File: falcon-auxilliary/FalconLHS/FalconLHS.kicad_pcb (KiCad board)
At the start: 2 copper layers, 85.7 x 57.5 mm, 18 parts, among them J1 100mil, U1 AL8843QSP-13, U2 AL8843QSP-13

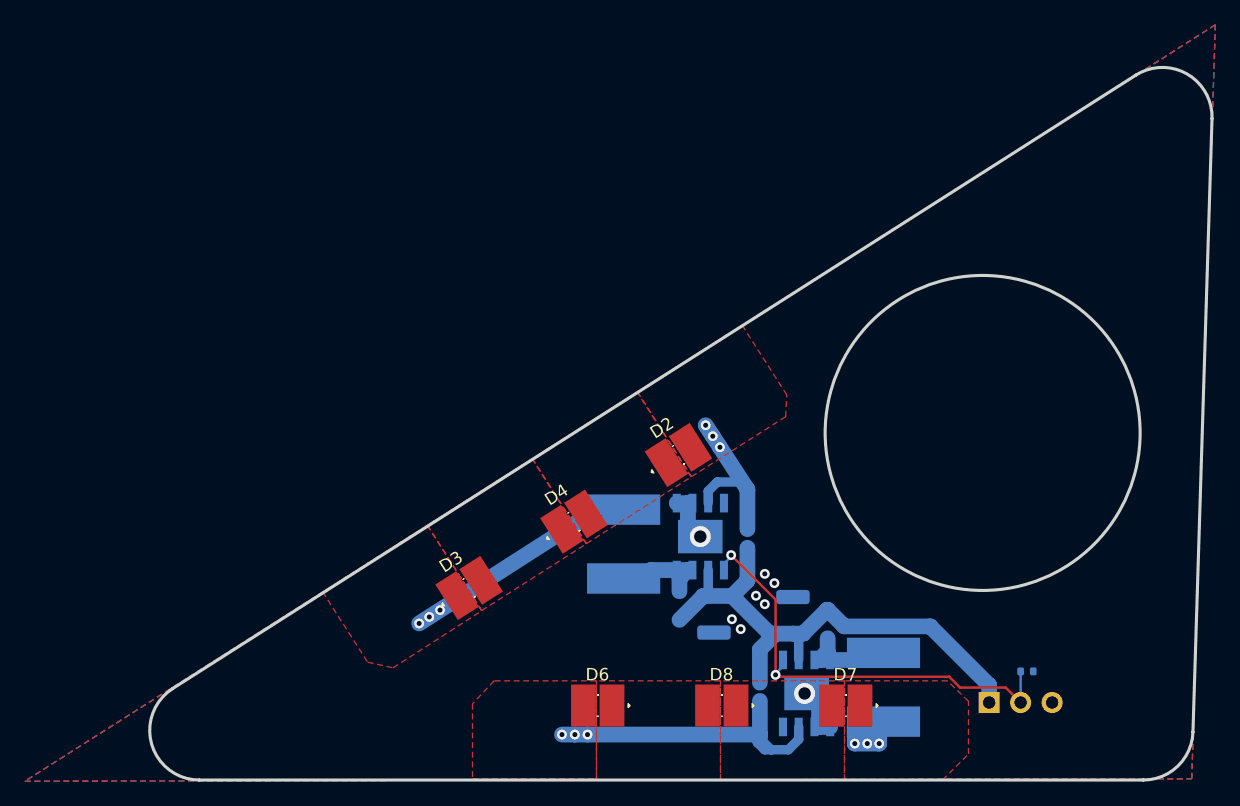
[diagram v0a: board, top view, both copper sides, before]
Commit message: Fix missing mounting holes
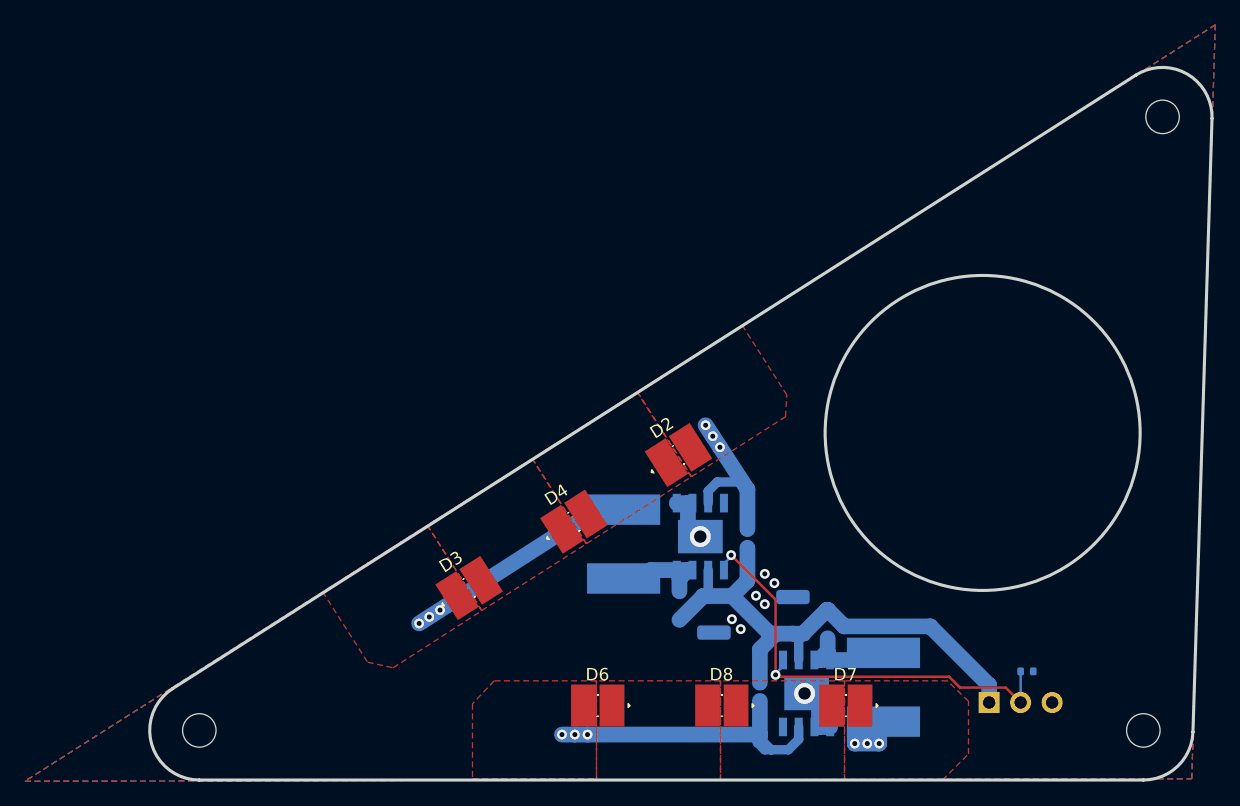
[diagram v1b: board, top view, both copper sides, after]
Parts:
- added H1: MountingHole, JetkovKiCADLib:MountingHole_2.7mm_M2.5_Clearanced, F.Cu at (109.0, 124.0)
- added H2: MountingHole, JetkovKiCADLib:MountingHole_2.7mm_M2.5_Clearanced, F.Cu at (186.7, 74.5)
- added H3: MountingHole, JetkovKiCADLib:MountingHole_2.7mm_M2.5_Clearanced, F.Cu at (185.1, 124.0)
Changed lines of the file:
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@@
     )
+  )
+  (footprint "JetkovKiCADLib:MountingHole_2.7mm_M2.5_Clearanced" locked (layer "F.Cu")
+    (at 185.125 124)
+    (descr "Mounting Hole 2.7mm, no annular, M2.5")
+    (tags "mounting hole 2.7mm no annular m2.5")
+    (property "Sheetfile" "FalconLHS.kicad_sch")
+    (property "Sheetname" "")
+    (clearance 1.5)
+    (attr exclude_from_pos_files)
+    (fp_text reference "H3" (at 0 -3.7) (layer "F.SilkS") hide
+      (effects (font (size 1 1) (thickness 0.15)))
+    )
+    (fp_text value "MountingHole" (at 0 3.7) (layer "F.Fab")
+      (effects (font (size 1 1) (thickness 0.15)))
+    )
+    (fp_text user "${REFERENCE}" (at 0.3 0) (layer "F.Fab")
+      (effects (font (size 1 1) (thickness 0.15)))
+    )
+    (fp_circle (center 0 0) (end 2.7 0) (layer "Cmts.User") (width 0.15) (fill none))
+    (fp_circle (center 0 0) (end 2.95 0) (layer "F.CrtYd") (width 0.05) (fill none))
+    (pad "" np_thru_hole circle locked (at 0 0) (size 2.7 2.7) (drill 2.7) (layers F&B.Cu *.Mask)
+      (clearance 1.5))
+  )
+  (footprint "JetkovKiCADLib:MountingHole_2.7mm_M2.5_Clearanced" locked (layer "F.Cu")
+    (at 186.675 74.525)
+    (descr "Mounting Hole 2.7mm, no annular, M2.5")
+    (tags "mounting hole 2.7mm no annular m2.5")
+    (property "Sheetfile" "FalconLHS.kicad_sch")
+    (property "Sheetname" "")
+    (clearance 1.5)
+    (attr exclude_from_pos_files)
+    (fp_text reference "H2" (at 0 -3.7) (layer "F.SilkS") hide
+      (effects (font (size 1 1) (thickness 0.15)))
+    )
+    (fp_text value "MountingHole" (at 0 3.7) (layer "F.Fab")
+      (effects (font (size 1 1) (thickness 0.15)))
+    )
+    (fp_text user "${REFERENCE}" (at 0.3 0) (layer "F.Fab")
+      (effects (font (size 1 1) (thickness 0.15)))
+    )
+    (fp_circle (center 0 0) (end 2.7 0) (layer "Cmts.User") (width 0.15) (fill none))
+    (fp_circle (center 0 0) (end 2.95 0) (layer "F.CrtYd") (width 0.05) (fill none))
+    (pad "" np_thru_hole circle locked (at 0 0) (size 2.7 2.7) (drill 2.7) (layers F&B.Cu *.Mask)
+      (clearance 1.5))
   )
   (footprint "JetkovKiCADLib:XQ-A-LED_Large" (layer "F.Cu")
@@
     )
   )
-  (footprint "JetkovKiCADLib:XQ-A-LED_Large" (layer "F.Cu")
+  (footprint "JetkovKiCADLib:MountingHole_2.7mm_M2.5_Clearanced" locked (layer "F.Cu")
+    (at 109 124)
+    (descr "Mounting Hole 2.7mm, no annular, M2.5")
+    (tags "mounting hole 2.7mm no annular m2.5")
+    (property "Sheetfile" "FalconLHS.kicad_sch")
+    (property "Sheetname" "")
+    (clearance 1.5)
+    (attr exclude_from_pos_files)
+    (fp_text reference "H1" (at 0 -3.7) (layer "F.SilkS") hide
+      (effects (font (size 1 1) (thickness 0.15)))
+    )
+    (fp_text value "MountingHole" (at 0 3.7) (layer "F.Fab")
+      (effects (font (size 1 1) (thickness 0.15)))
+    )
+    (fp_text user "${REFERENCE}" (at 0.3 0) (layer "F.Fab")
+      (effects (font (size 1 1) (thickness 0.15)))
+    )
+    (fp_circle (center 0 0) (end 2.7 0) (layer "Cmts.User") (width 0.15) (fill none))
+    (fp_circle (center 0 0) (end 2.95 0) (layer "F.CrtYd") (width 0.05) (fill none))
+    (pad "" np_thru_hole circle locked (at 0 0) (size 2.7 2.7) (drill 2.7) (layers F&B.Cu *.Mask)
+      (clearance 1.5))
+  )
+  (footprint "JetkovKiCADLib:XQ-A-LED_Large" (layer "F.Cu")
